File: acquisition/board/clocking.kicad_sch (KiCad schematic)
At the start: 59 parts, among them U11 LMK04806, U12 AK5DAF1-100.0000T2, U14 74AVCH1T45, U15 74AVCH1T45, U16 74AVCH1T45, U17 74AVCH1T45, U19 74AVCH1T45, U20 74AVCH1T45

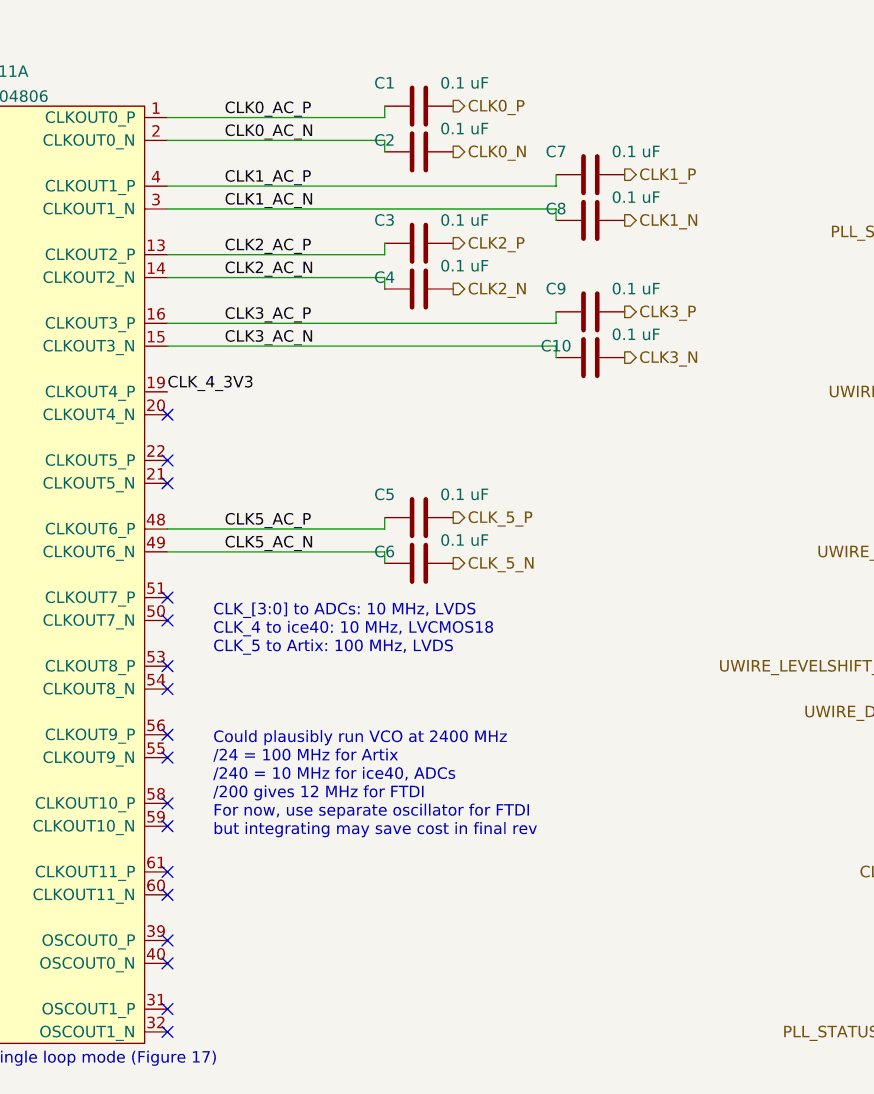
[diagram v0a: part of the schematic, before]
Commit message: Continued layout of clocking subsystem, second ADC, and BGA fanout
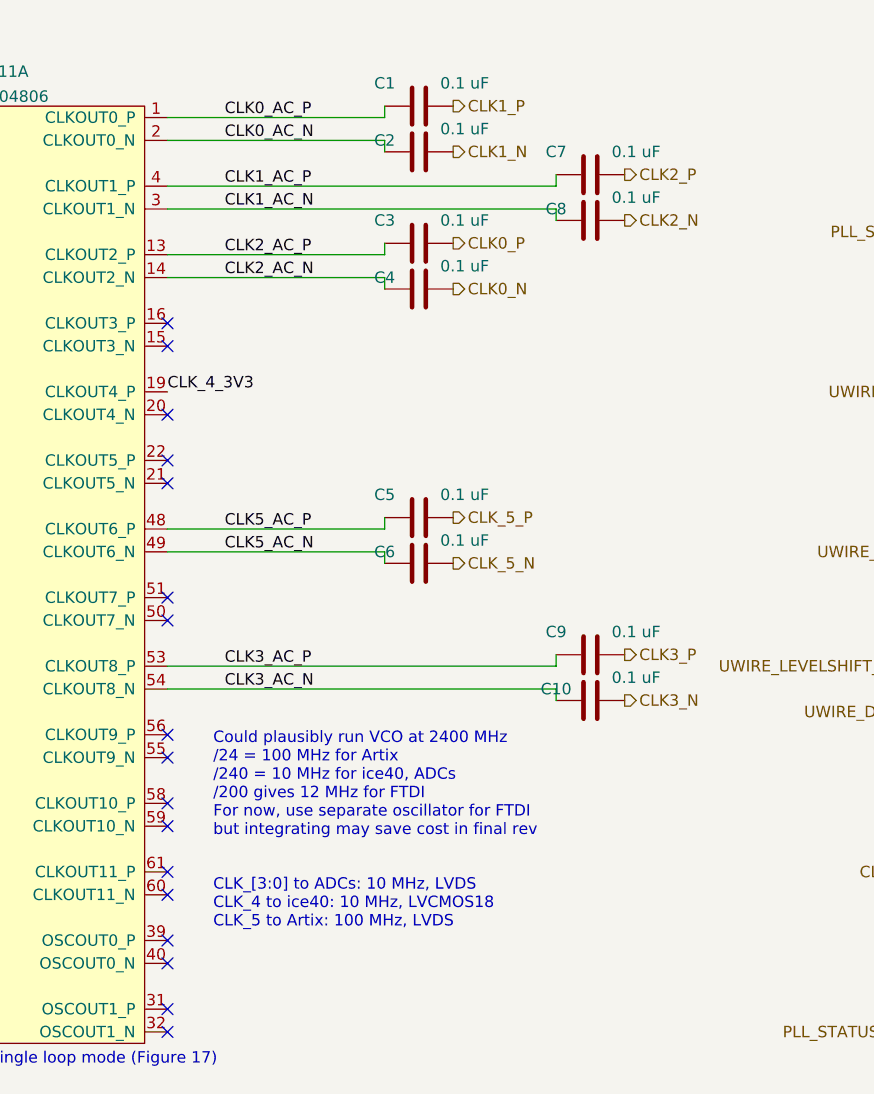
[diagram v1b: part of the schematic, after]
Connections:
- net CLK0_N: now also C4.2; no longer C2.2
- net CLK0_P: now also C3.2; no longer C1.2
- net CLK1_N: now also C2.2; no longer C8.2
- net CLK1_P: now also C1.2; no longer C7.2
- net CLK2_N: now also C8.2; no longer C4.2
- net CLK2_P: now also C7.2; no longer C3.2
- net CLK3_AC_N: now also U11.54 (CLKOUT8_N); no longer U11.15 (CLKOUT3_N)
- net CLK3_AC_P: now also U11.53 (CLKOUT8_P); no longer U11.16 (CLKOUT3_P)
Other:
- moved on the sheet: C10, C9
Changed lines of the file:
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@@
   (no_connect (at 113.03 35.56))
   (no_connect (at 107.95 148.59))
+  (no_connect (at 148.59 81.28))
+  (no_connect (at 148.59 78.74))
   (no_connect (at 148.59 66.04))
   (no_connect (at 148.59 119.38))
   (no_connect (at 148.59 124.46))
   (no_connect (at 148.59 127))
-  (no_connect (at 148.59 81.28))
-  (no_connect (at 148.59 86.36))
+  (no_connect (at 148.59 48.26))
+  (no_connect (at 148.59 50.8))
   (no_connect (at 148.59 58.42))
   (no_connect (at 148.59 63.5))
@@
   (no_connect (at 148.59 101.6))
   (no_connect (at 148.59 93.98))
-  (no_connect (at 148.59 88.9))
   (no_connect (at 148.59 96.52))
-  (no_connect (at 148.59 78.74))
   (no_connect (at 113.03 33.02))
   (wire (pts (xy 90.17 45.72) (xy 97.79 45.72))
@@
     (stroke (width 0) (type default) (color 0 0 0 0))
   )
-  (wire (pts (xy 191.77 48.26) (xy 191.77 46.99))
+  (wire (pts (xy 191.77 86.36) (xy 191.77 85.09))
     (stroke (width 0) (type default) (color 0 0 0 0))
   )
@@
     (stroke (width 0) (type default) (color 0 0 0 0))
   )
-  (wire (pts (xy 148.59 48.26) (xy 191.77 48.26))
+  (wire (pts (xy 148.59 86.36) (xy 191.77 86.36))
     (stroke (width 0) (type default) (color 0 0 0 0))
   )
@@
     (stroke (width 0) (type default) (color 0 0 0 0))
   )
-  (wire (pts (xy 148.59 50.8) (xy 191.77 50.8))
+  (wire (pts (xy 148.59 88.9) (xy 191.77 88.9))
     (stroke (width 0) (type default) (color 0 0 0 0))
   )
@@
     (stroke (width 0) (type default) (color 0 0 0 0))
   )
-  (wire (pts (xy 191.77 50.8) (xy 191.77 52.07))
+  (wire (pts (xy 191.77 88.9) (xy 191.77 90.17))
     (stroke (width 0) (type default) (color 0 0 0 0))
   )
@@
   )
   (text "CLK_[3:0] to ADCs: 10 MHz, LVDS\nCLK_4 to ice40: 10 MHz, LVCMOS18\nCLK_5 to Artix: 100 MHz, LVDS"
-    (at 153.67 85.09 0)
+    (at 153.67 115.57 0)
     (effects (font (size 1.27 1.27)) (justify left bottom))
   )
@@
     (effects (font (size 1.27 1.27)) (justify right bottom))
   )
-  (label "CLK3_AC_N" (at 154.94 50.8 0)
+  (label "CLK3_AC_N" (at 154.94 88.9 0)
     (effects (font (size 1.27 1.27)) (justify left bottom))
   )
@@
     (effects (font (size 1.27 1.27)) (justify left bottom))
   )
-  (label "CLK3_AC_P" (at 154.94 48.26 0)
+  (label "CLK3_AC_P" (at 154.94 86.36 0)
     (effects (font (size 1.27 1.27)) (justify left bottom))
   )
@@
     (effects (font (size 1.27 1.27)) (justify right))
   )
-  (hierarchical_label "CLK1_N" (shape output) (at 199.39 36.83 0)
+  (hierarchical_label "CLK1_N" (shape output) (at 180.34 29.21 0)
     (effects (font (size 1.27 1.27)) (justify left))
   )
-  (hierarchical_label "CLK1_P" (shape output) (at 199.39 31.75 0)
+  (hierarchical_label "CLK1_P" (shape output) (at 180.34 24.13 0)
     (effects (font (size 1.27 1.27)) (justify left))
   )
@@
     (effects (font (size 1.27 1.27)) (justify right))
   )
-  (hierarchical_label "CLK2_N" (shape output) (at 180.34 44.45 0)
+  (hierarchical_label "CLK2_N" (shape output) (at 199.39 36.83 0)
     (effects (font (size 1.27 1.27)) (justify left))
   )
@@
     (effects (font (size 1.27 1.27)) (justify right))
   )
-  (hierarchical_label "CLK3_N" (shape output) (at 199.39 52.07 0)
+  (hierarchical_label "CLK3_N" (shape output) (at 199.39 90.17 0)
     (effects (font (size 1.27 1.27)) (justify left))
   )
@@
     (effects (font (size 1.27 1.27)) (justify right))
   )
-  (hierarchical_label "CLK2_P" (shape output) (at 180.34 39.37 0)
+  (hierarchical_label "CLK2_P" (shape output) (at 199.39 31.75 0)
     (effects (font (size 1.27 1.27)) (justify left))
   )
-  (hierarchical_label "CLK3_P" (shape output) (at 199.39 46.99 0)
+  (hierarchical_label "CLK3_P" (shape output) (at 199.39 85.09 0)
     (effects (font (size 1.27 1.27)) (justify left))
   )
-  (hierarchical_label "CLK0_N" (shape output) (at 180.34 29.21 0)
+  (hierarchical_label "CLK0_N" (shape output) (at 180.34 44.45 0)
     (effects (font (size 1.27 1.27)) (justify left))
   )
-  (hierarchical_label "CLK0_P" (shape output) (at 180.34 24.13 0)
+  (hierarchical_label "CLK0_P" (shape output) (at 180.34 39.37 0)
     (effects (font (size 1.27 1.27)) (justify left))
   )
@@
     (pin "2")
   )
-  (symbol (lib_id "device:C") (at 195.58 46.99 90) (unit 1)
+  (symbol (lib_id "device:C") (at 195.58 85.09 90) (unit 1)
     (in_bom yes) (on_board yes)
-    (property "Reference" "C9" (id 0) (at 191.77 44.45 90))
-    (property "Value" "0.1 uF" (id 1) (at 200.66 44.45 90))
-    (property "Footprint" "azonenberg_pcb:EIA_0402_CAP_NOSILK" (id 2) (at 199.39 46.0248 0)
-      (effects (font (size 1.27 1.27)) hide)
-    )
-    (property "Datasheet" "" (id 3) (at 195.58 46.99 0)
+    (property "Reference" "C9" (id 0) (at 191.77 82.55 90))
+    (property "Value" "0.1 uF" (id 1) (at 200.66 82.55 90))
+    (property "Footprint" "azonenberg_pcb:EIA_0402_CAP_NOSILK" (id 2) (at 199.39 84.1248 0)
+      (effects (font (size 1.27 1.27)) hide)
+    )
+    (property "Datasheet" "" (id 3) (at 195.58 85.09 0)
       (effects (font (size 1.27 1.27)) hide)
     )
@@
     (pin "2")
   )
-  (symbol (lib_id "device:C") (at 195.58 52.07 90) (unit 1)
+  (symbol (lib_id "device:C") (at 195.58 90.17 90) (unit 1)
     (in_bom yes) (on_board yes)
-    (property "Reference" "C10" (id 0) (at 191.77 50.8 90))
-    (property "Value" "0.1 uF" (id 1) (at 200.66 49.53 90))
-    (property "Footprint" "azonenberg_pcb:EIA_0402_CAP_NOSILK" (id 2) (at 199.39 51.1048 0)
-      (effects (font (size 1.27 1.27)) hide)
-    )
-    (property "Datasheet" "" (id 3) (at 195.58 52.07 0)
-      (effects (font (size 1.27 1.27)) hide)
-    )
+    (property "Reference" "C10" (id 0) (at 191.77 88.9 90))
+    (property "Value" "0.1 uF" (id 1) (at 200.66 87.63 90))
+    (property "Footprint" "azonenberg_pcb:EIA_0402_CAP_NOSILK" (id 2) (at 199.39 89.2048 0)
+      (effects (font (size 1.27 1.27)) hide)
+    )
+    (property "Datasheet" "" (id 3) (at 195.58 90.17 0)
+      (effects (font (size 1.27 1.27)) hide)
+    )
